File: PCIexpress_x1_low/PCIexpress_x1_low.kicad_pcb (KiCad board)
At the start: 4 copper layers, 167.7 x 68.9 mm, 6 parts, among them J1 PCIexpress_bracket, J2 PCIexpress_x1

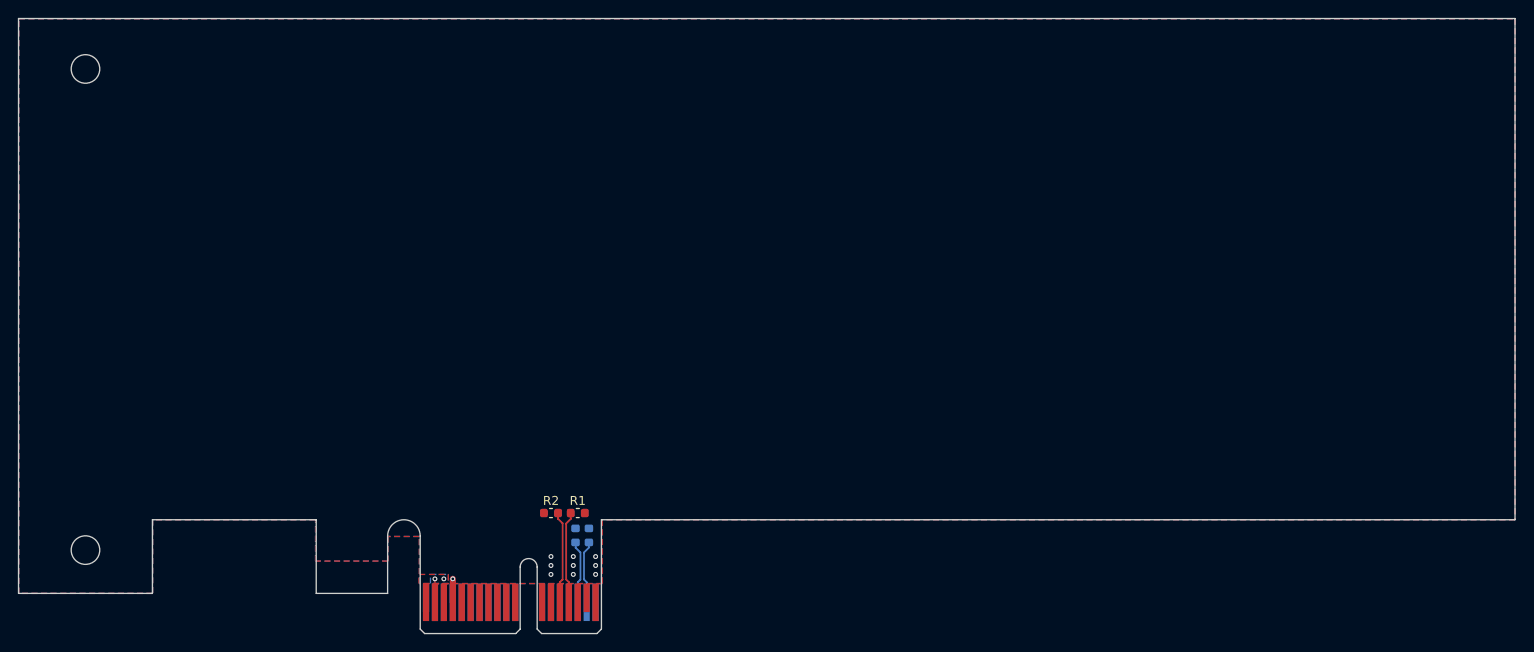
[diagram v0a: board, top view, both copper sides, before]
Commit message: working to route 0.8mm pitch bga, probably not practical
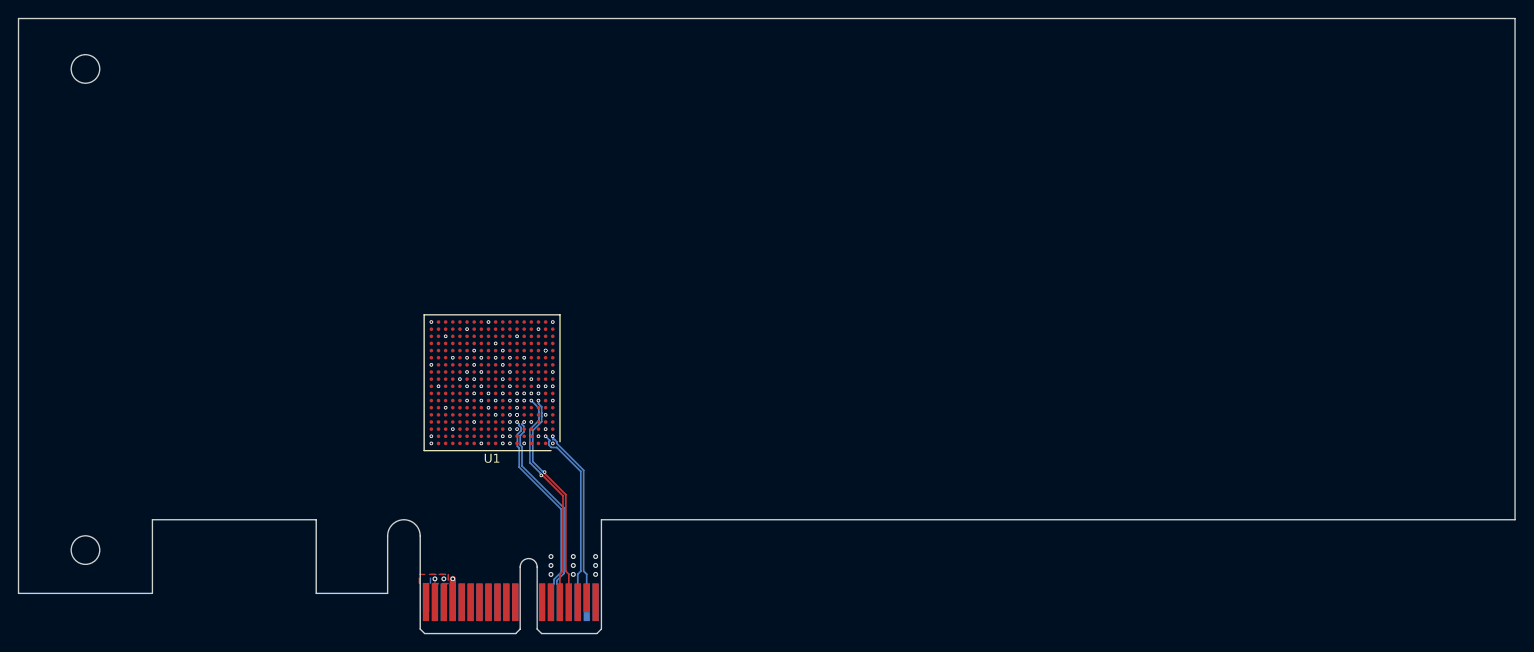
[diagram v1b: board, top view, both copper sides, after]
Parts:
- removed C1, C2: 100n, Capacitor_SMD:C_0603_1608Metric
- removed R1, R2: 49.9, Resistor_SMD:R_0603_1608Metric
- added U1: XC7A50T-CSG325, Package_BGA:Xilinx_CSG325, F.Cu at (117.5, 166.0)
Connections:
- J2 pad A16: /PCIexpress_connector/_PER0_P -> /PER0_P
- J2 pad A17: /PCIexpress_connector/_PER0_N -> /PER0_N
- J2 pad B12: Net-(J2-PadB12) -> unconnected-(J2-RSVD-PadB12)
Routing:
- net /REFCLK+: track 0.00 -> 23.1 mm, vias 0 -> 1
- net /REFCLK-: track 0.00 -> 23.1 mm, vias 0 -> 1
- net /PER0_P: track 0.00 -> 20.9 mm, vias 0 -> 1
- net /PER0_N: track 0.00 -> 20.3 mm, vias 0 -> 1
- net /PET0_P: track 10.3 -> 25.1 mm, vias 0 -> 2
- net /PET0_N: track 10.3 -> 24.9 mm, vias 0 -> 2
- net /PCIexpress_connector/_PER0_P: track 7.06 -> 0.00 mm
- net /PCIexpress_connector/_PER0_N: track 7.06 -> 0.00 mm
- net GND: vias 10 -> 85
- added copper zone on In4.Cu, net GND
- removed copper zone on B.Cu, net GND
- removed copper zone on F.Cu, net GND
- removed copper zone on In2.Cu, net GND
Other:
- copper layers 4 -> 6

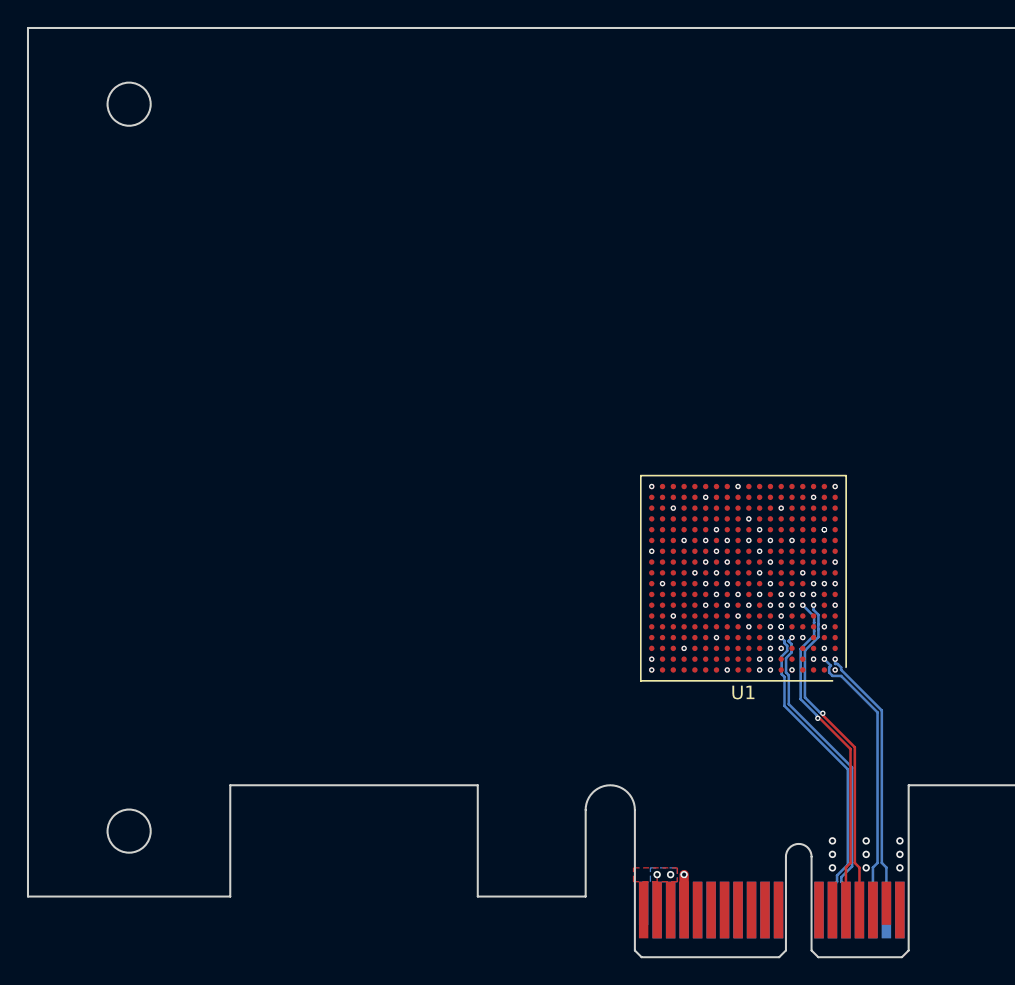
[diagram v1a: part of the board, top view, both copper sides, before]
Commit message: looks liket the xilinx csg325 package can route in Oshpark 6 layer stackup
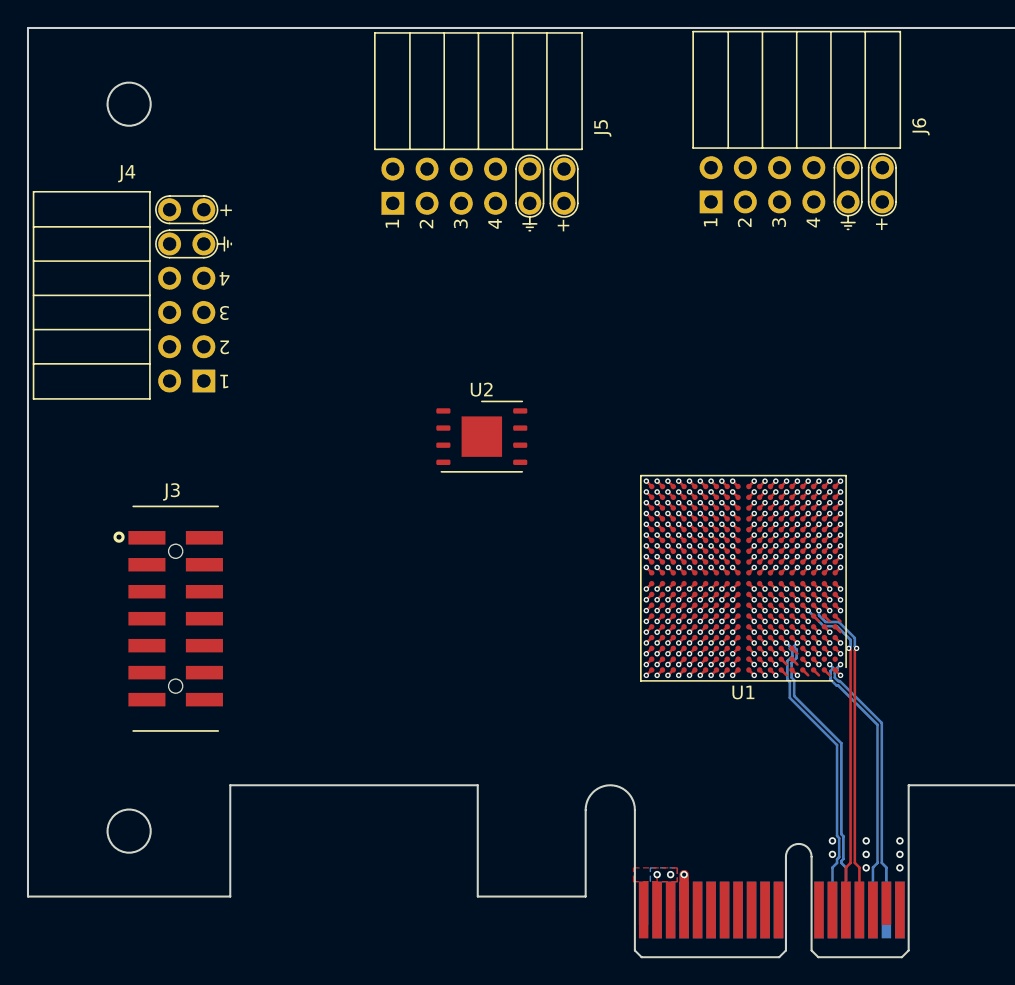
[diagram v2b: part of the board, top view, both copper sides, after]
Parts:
- added J3: 87832-1420, pedrolib:MOLEX_87832-1420, F.Cu at (75.4, 169.0)
- added J4: PMOD_Host_Conn_02x06, pedrolib:PMOD_PinSocket_2x06_P2.54mm_Horizontal, F.Cu at (77.5, 151.4)
- added J5: PMOD_Host_Conn_02x06, pedrolib:PMOD_PinSocket_2x06_P2.54mm_Horizontal, F.Cu at (91.5, 138.2)
- added J6: PMOD_Host_Conn_02x06, pedrolib:PMOD_PinSocket_2x06_P2.54mm_Horizontal, F.Cu at (115.1, 138.1)
- added U2: MT25QUxxxxxx1xW7, Package_DFN_QFN:W-PDFN-8-1EP_6x5mm_P1.27mm_EP3x3mm, F.Cu at (98.1, 155.5)
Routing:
- net GND: track 2.62 -> 45.1 mm, vias 85 -> 84
- net /PER0_P: track 20.9 -> 20.0 mm
- net /REFCLK-: track 23.1 -> 22.5 mm
- net /REFCLK+: track 23.1 -> 22.5 mm
- net unconnected-(U1F-VCCINT-PadP9): track 0.00 -> 0.57 mm, vias 0 -> 1
- net unconnected-(U1F-VCCINT-PadP11): track 0.00 -> 0.57 mm, vias 0 -> 1
- net unconnected-(U1F-VCCINT-PadN8): track 0.00 -> 0.57 mm, vias 0 -> 1
- net unconnected-(U1F-VCCINT-PadN12): track 0.00 -> 0.57 mm, vias 0 -> 1
- net unconnected-(U1F-VCCINT-PadN10): track 0.00 -> 0.57 mm, vias 0 -> 1
- net unconnected-(U1F-VCCINT-PadM11): track 0.00 -> 0.57 mm, vias 0 -> 1
- net unconnected-(U1F-VCCINT-PadK11): track 0.00 -> 0.57 mm, vias 0 -> 1
- net unconnected-(U1F-VCCINT-PadH9): track 0.00 -> 0.57 mm, vias 0 -> 1
- net unconnected-(U1F-VCCINT-PadG8): track 0.00 -> 0.57 mm, vias 0 -> 1
- net unconnected-(U1F-VCCINT-PadF9): track 0.00 -> 0.57 mm, vias 0 -> 1
- net unconnected-(U1F-VCCBRAM-PadH11): track 0.00 -> 0.57 mm, vias 0 -> 1
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
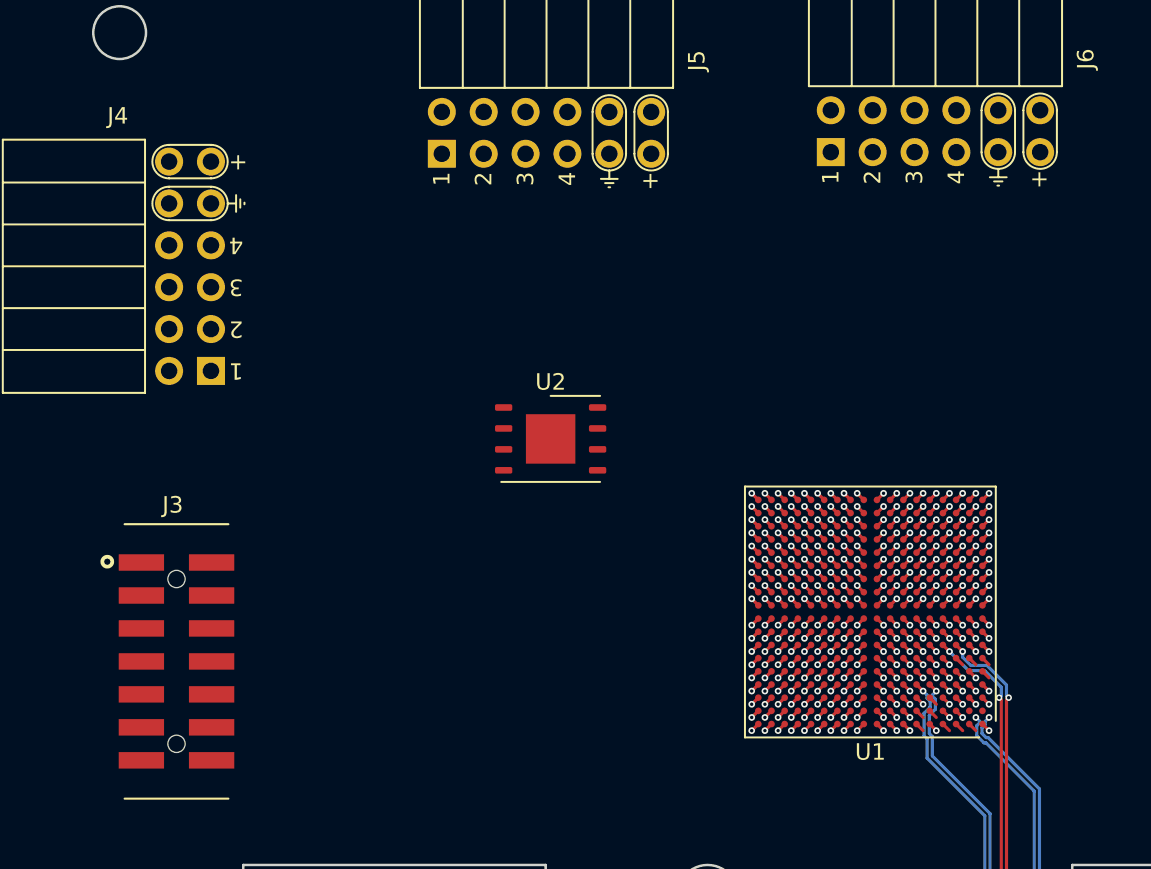
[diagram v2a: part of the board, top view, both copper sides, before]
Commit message: added pmic and config flash
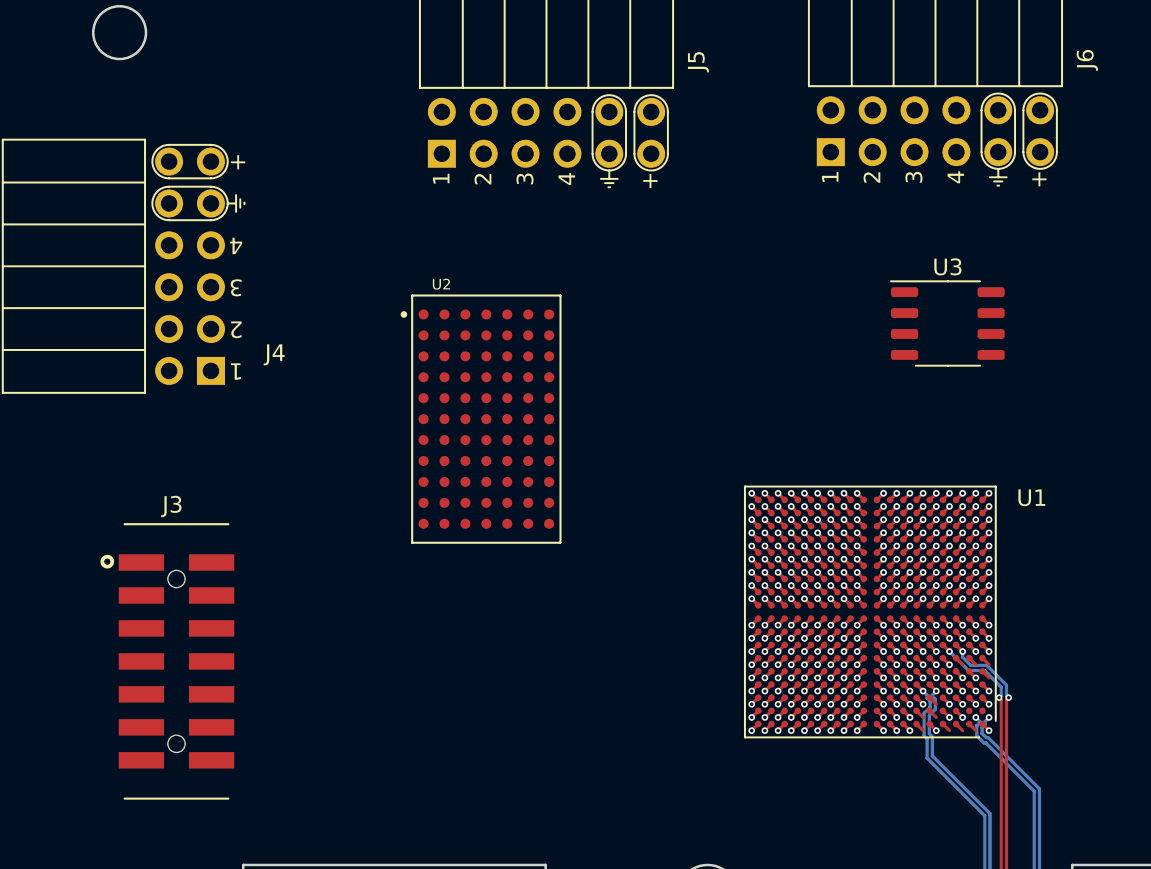
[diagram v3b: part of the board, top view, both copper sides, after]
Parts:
- added U3: MX25L3233FM1, Package_SO:SOP-8_3.9x4.9mm_P1.27mm, F.Cu at (122.2, 148.5)
- U2: value MT25QUxxxxxx1xW7 -> LTM4643EY_PBF; footprint Package_DFN_QFN:W-PDFN-8-1EP_6x5mm_P1.27mm_EP3x3mm -> pedrolib:BGA77C127P7X11_1500X900X262
- moved U2 4.08 mm to (94.2, 154.3)

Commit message: threw down some LEDs
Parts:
- added D1: LED, LED_SMD:LED_0603_1608Metric, F.Cu at (136.2, 149.3)
- added D2: LED, LED_SMD:LED_0603_1608Metric, F.Cu at (136.2, 151.9)
- added D3: LED, LED_SMD:LED_0603_1608Metric, F.Cu at (136.2, 154.5)
- added D4: LED, LED_SMD:LED_0603_1608Metric, F.Cu at (136.2, 157.1)
- added D5: LED, LED_SMD:LED_0603_1608Metric, F.Cu at (136.2, 159.7)
- added D6: LED, LED_SMD:LED_0603_1608Metric, F.Cu at (136.2, 162.2)
- added D7: LED, LED_SMD:LED_0603_1608Metric, F.Cu at (136.2, 164.8)
- added D8: LED, LED_SMD:LED_0603_1608Metric, F.Cu at (136.2, 167.4)
- added R1: R, Resistor_SMD:R_0603_1608Metric, F.Cu at (145.2, 149.0)
- added R2: R, Resistor_SMD:R_0603_1608Metric, F.Cu at (145.2, 151.5)
- added R3: R, Resistor_SMD:R_0603_1608Metric, F.Cu at (145.2, 154.0)
- added R4: R, Resistor_SMD:R_0603_1608Metric, F.Cu at (145.2, 156.5)
- added R5: R, Resistor_SMD:R_0603_1608Metric, F.Cu at (145.2, 159.0)
- added R6: R, Resistor_SMD:R_0603_1608Metric, F.Cu at (145.2, 161.5)
- added R7: R, Resistor_SMD:R_0603_1608Metric, F.Cu at (145.2, 164.0)
- added R8: R, Resistor_SMD:R_0603_1608Metric, F.Cu at (145.2, 166.5)

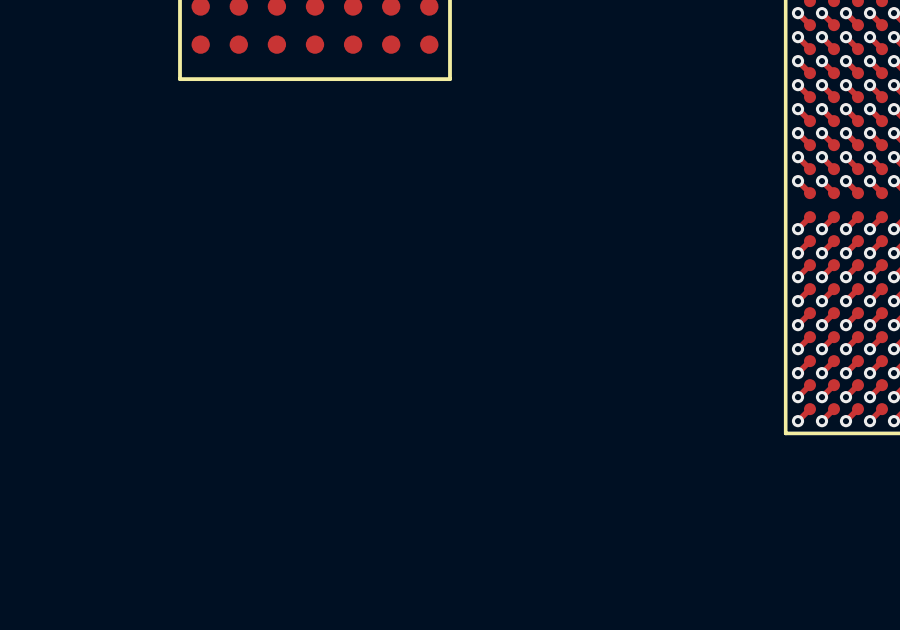
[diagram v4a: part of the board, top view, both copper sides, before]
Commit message: adding AC coupling caps
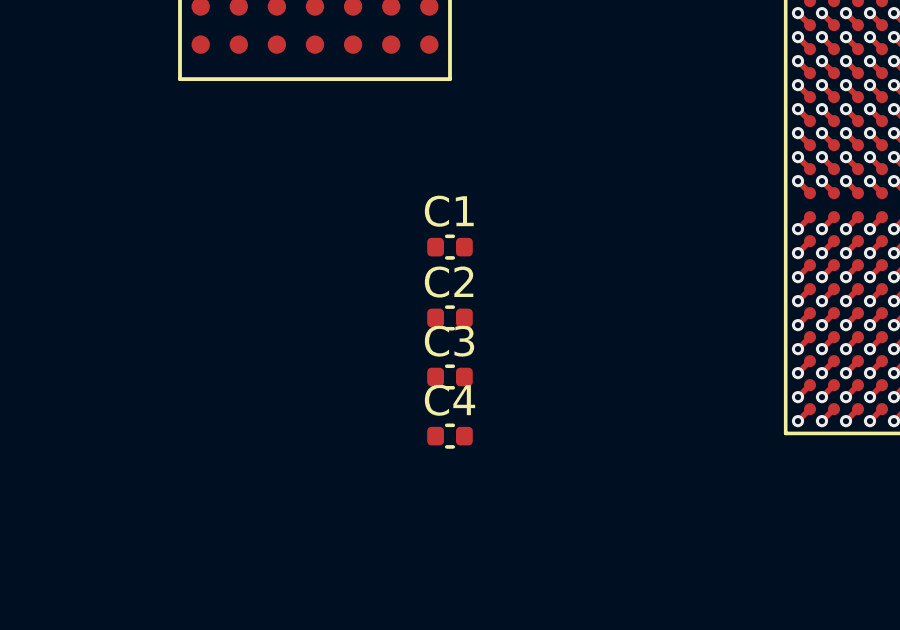
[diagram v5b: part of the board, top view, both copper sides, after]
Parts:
- added C1: C, Capacitor_SMD:C_0402_1005Metric, F.Cu at (98.7, 167.4)
- added C2: C, Capacitor_SMD:C_0402_1005Metric, F.Cu at (98.7, 169.8)
- added C3: C, Capacitor_SMD:C_0402_1005Metric, F.Cu at (98.7, 171.8)
- added C4: C, Capacitor_SMD:C_0402_1005Metric, F.Cu at (98.7, 173.7)
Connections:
- net /~{PERST} renamed /perstn
- net /~{WAKE} renamed /waken
- J2 pad A1: /~{PRSNT1} -> /prsntn
- J2 pad A10: +3V3 -> unconnected-(J2-+3.3V-PadA10)
- J2 pad A16: /PER0_P -> /PET0_P
- J2 pad A17: /PER0_N -> /PET0_N
- J2 pad A5: /TCK -> unconnected-(J2-TCK-PadA5)
- J2 pad A6: /TDI -> unconnected-(J2-TDI-PadA6)
- J2 pad A7: /TDO -> unconnected-(J2-TDO-PadA7)
- J2 pad A8: /TMS -> unconnected-(J2-TMS-PadA8)
- J2 pad A9: +3V3 -> unconnected-(J2-+3.3V-PadA9)
- J2 pad B10: +3.3VA -> unconnected-(J2-+3.3V_aux-PadB10)
- J2 pad B14: /PET0_P -> /PER0_P
- J2 pad B15: /PET0_N -> /PER0_N
- J2 pad B17: /~{PRSNT2x1} -> /prsntn
- J2 pad B5: /SMCLK -> unconnected-(J2-SMCLK-PadB5)
- J2 pad B6: /SMDAT -> unconnected-(J2-SMDAT-PadB6)
- J2 pad B8: +3V3 -> unconnected-(J2-+3.3V-PadB8)
- J2 pad B9: /~{TRST} -> unconnected-(J2-~{TRST}-PadB9)
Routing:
- net /PET0_N: track 24.7 -> 44.7 mm, vias 2 -> 3
- net /PER0_N: track 20.0 -> 0.00 mm, vias 1 -> 0
- net /PET0_P: track 24.9 -> 44.9 mm, vias 2 -> 3
- net /PER0_P: track 20.0 -> 0.00 mm, vias 1 -> 0
- net +12V: vias 2 -> 1
- net (no net): vias 0 -> 1
- added copper zone on B.Cu, net (none)
- added copper zone on F.Cu, net (none)
- removed copper zone on B.Cu, net +12V
- removed copper zone on F.Cu, net +12V
